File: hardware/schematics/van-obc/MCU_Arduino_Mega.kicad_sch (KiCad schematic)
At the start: 2 parts

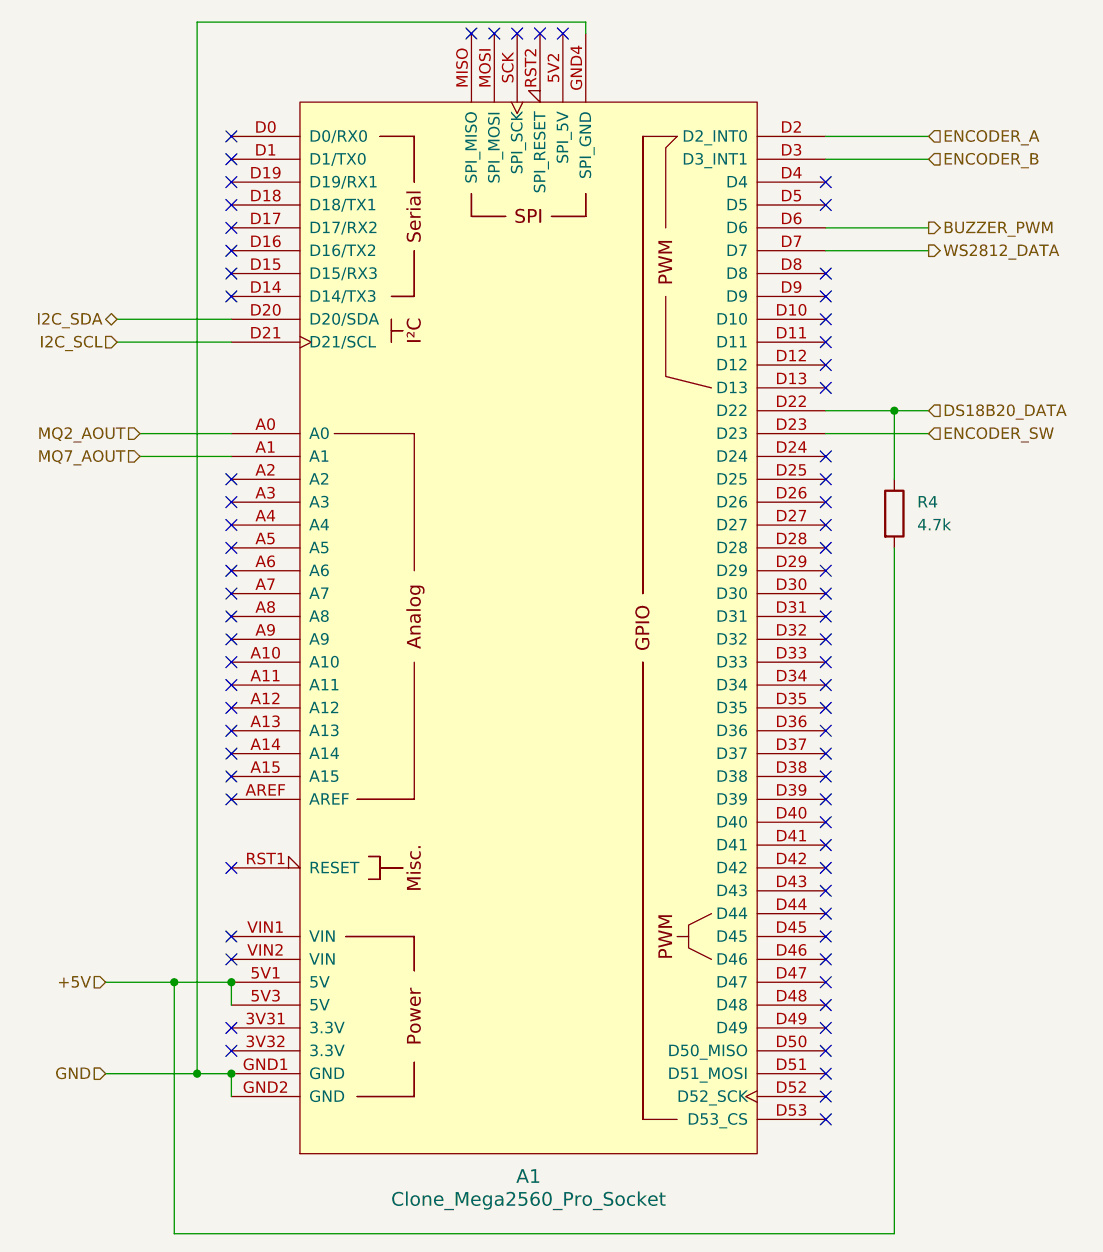
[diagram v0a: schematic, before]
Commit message: fix(tests): Corrections majeures KY040, BME280, MPU6050
- KY040 v2.1.0: Fix comptage + anti-rebond capacitif
- BME280 v1.0.1: Fix begin() avec &Wire
- MPU6050 v2.0.0: Simplification (acc only, dérive <2°)
- Ajout diagnostic_bme280.ino + CHANGELOG

Tests: 6/11 validés (55%)
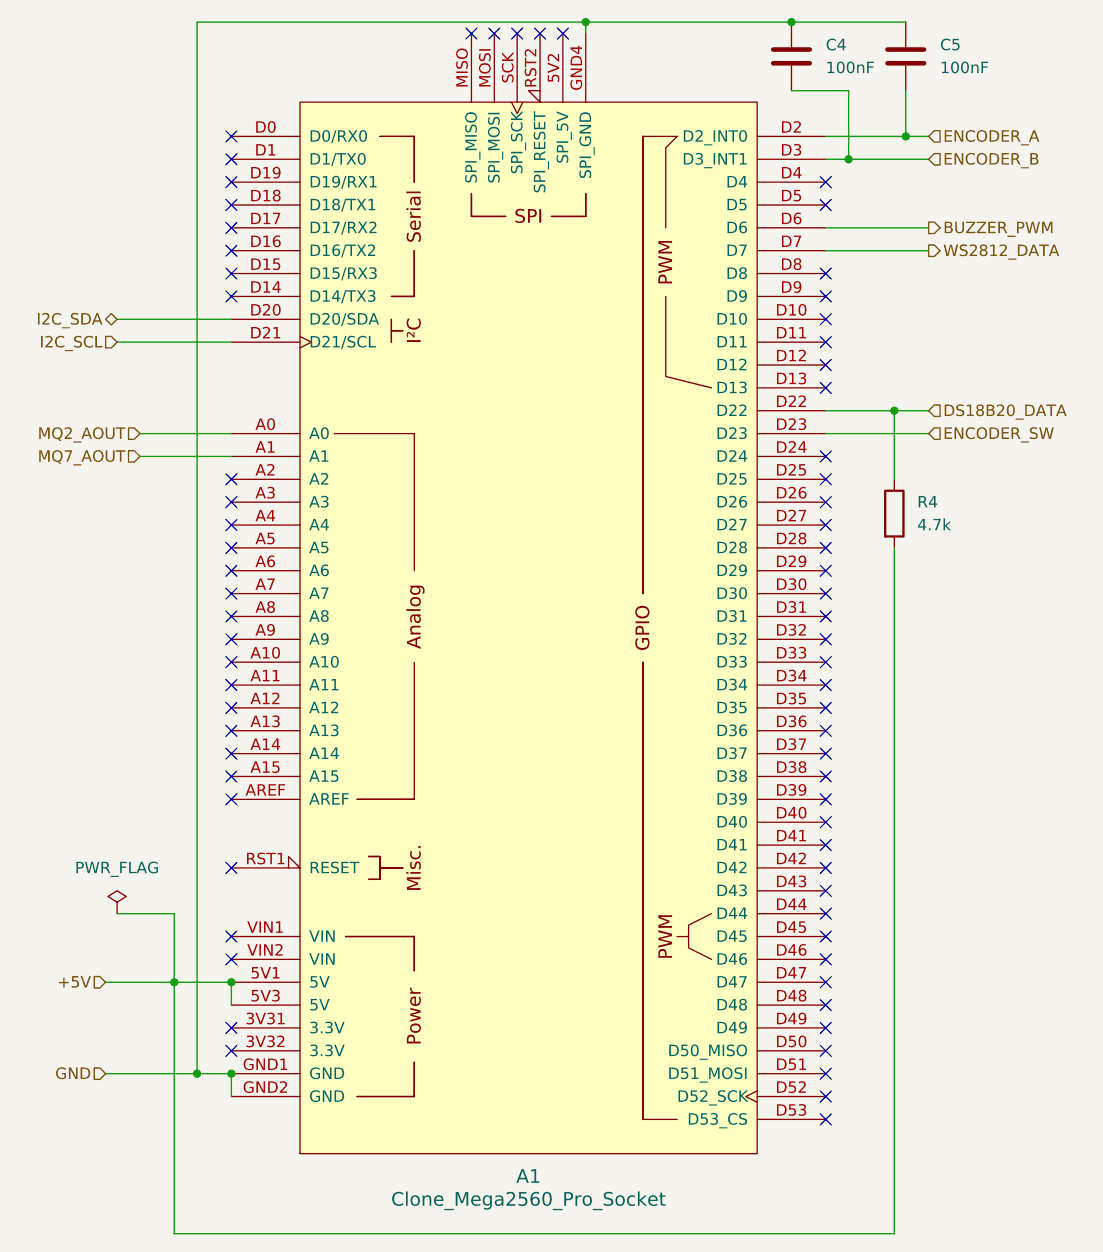
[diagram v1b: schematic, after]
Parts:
- added C4, C5: 100nF, Capacitor_THT:C_Disc_D4.3mm_W1.9mm_P5.00mm, symbol Device:C
- R4: footprint (none) -> Resistor_THT:R_Axial_DIN0207_L6.3mm_D2.5mm_P10.16mm_Horizontal
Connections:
- net ENCODER_A: now also C5.2
- net ENCODER_B: now also C4.2
- net GND: now also C4.1, C5.1
